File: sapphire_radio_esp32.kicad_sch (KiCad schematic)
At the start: 137 parts, among them IC1 AZ1117CH-3.3TRG1, IC2 AS169-73LF, IC3 CP2102N-A02-GQFN28R, J1 GT-USB-7055E, J2 Screw_Terminal_01x02, J3 FAKRA, J4 Screw_Terminal_01x02, J5 Screw_Terminal_01x02, J6 Conn_01x03, Q1 DMG2305UX-7, Q2 DMP3013SFV-7, Q3 2N7002PS_115, SW1 1825027-8, SW2 1825027-8, SW3 1825027-8, SW4 1825027-8, SW5 1825027-8, SW6 RK09711110EL, U1 ESP32-WROOM-32E-N8R2, U3 NC7WZ14P6X, U4 SI4735, U5 NC7WZ14P6X, U6 TMUX1574PWR, U7 PCM5122PWR, U8 MAX9744ETH_

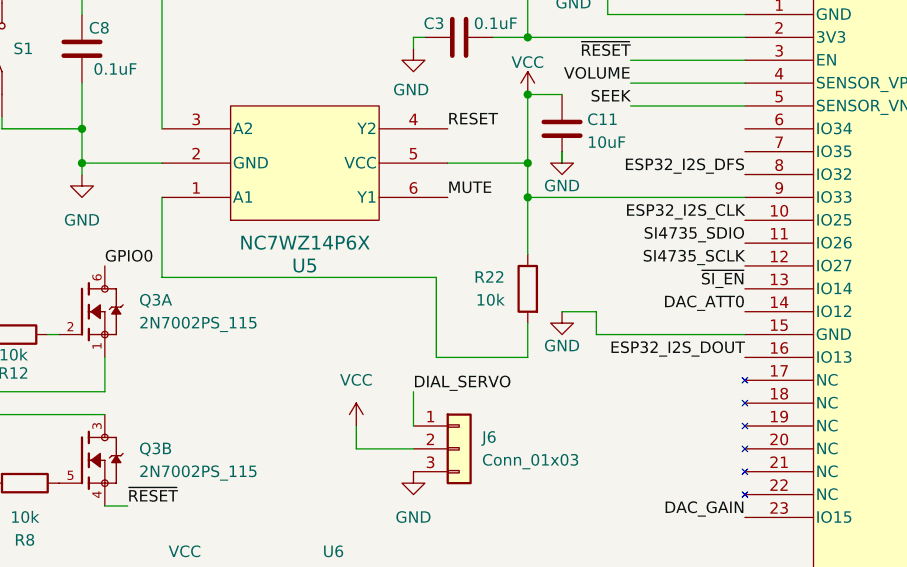
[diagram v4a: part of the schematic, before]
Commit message: Move fakra to board edge; move associated parts; silkscreen
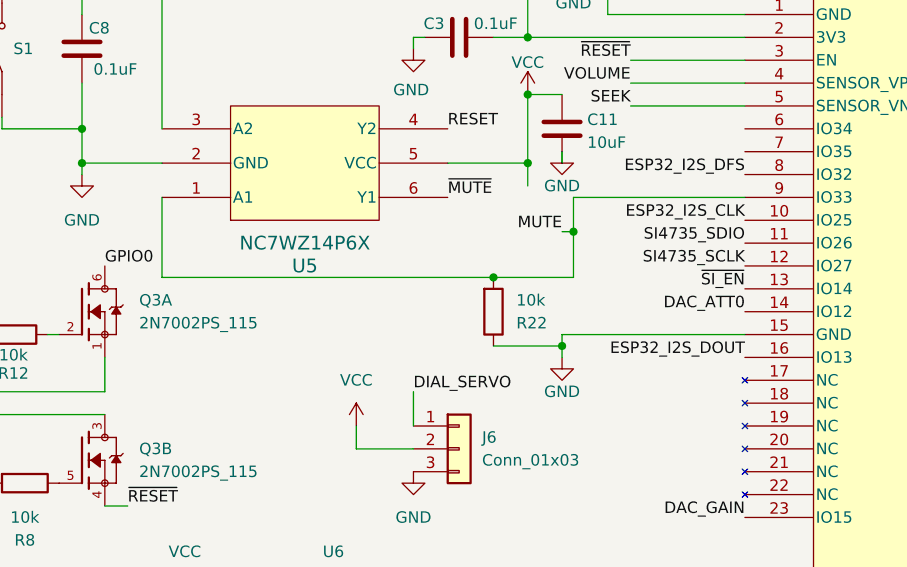
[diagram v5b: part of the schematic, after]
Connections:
- net GND: now also R22.1
- net MUTE: now also R22.2, U1.9 (IO33), U5.1 (A1); no longer U5.6 (Y1)
- net VCC: no longer R22.1, U1.9 (IO33)
- net ~{MUTE}: now also U5.6 (Y1)
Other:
- moved on the sheet: R22
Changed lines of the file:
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@@
 	)
 	(junction
+		(at 76.2 124.46)
+		(diameter 0)
+		(color 0 0 0 0)
+	)
+	(junction
 		(at 80.01 111.76)
 		(diameter 0)
@@
 	)
 	(junction
-		(at 80.01 115.57)
-		(diameter 0)
-		(color 0 0 0 0)
-	)
-	(junction
 		(at 30.48 90.17)
 		(diameter 0)
@@
 	)
 	(junction
+		(at 85.09 119.38)
+		(diameter 0)
+		(color 0 0 0 0)
+	)
+	(junction
 		(at 299.72 17.78)
 		(diameter 0)
@@
 	)
 	(junction
+		(at 83.82 132.08)
+		(diameter 0)
+		(color 0 0 0 0)
+	)
+	(junction
 		(at 167.64 68.58)
 		(diameter 0)
@@
 	(wire
 		(pts
-			(xy 87.63 128.27) (xy 87.63 130.81)
-		)
-		(stroke
-			(width 0)
-			(type default)
-		)
-	)
-	(wire
-		(pts
 			(xy 38.1 43.18) (xy 45.72 43.18)
 		)
@@
 	(wire
 		(pts
+			(xy 83.82 133.35) (xy 83.82 132.08)
+		)
+		(stroke
+			(width 0)
+			(type default)
+		)
+	)
+	(wire
+		(pts
 			(xy 232.41 20.32) (xy 233.68 20.32)
 		)
@@
 	(wire
 		(pts
-			(xy 39.37 124.46) (xy 69.85 124.46)
-		)
-		(stroke
-			(width 0)
-			(type default)
-		)
-	)
-	(wire
-		(pts
-			(xy 69.85 133.35) (xy 80.01 133.35)
+			(xy 203.2 88.9) (xy 213.36 88.9)
 		)
 		(stroke
@@
 	(wire
 		(pts
-			(xy 203.2 88.9) (xy 213.36 88.9)
+			(xy 232.41 33.02) (xy 234.95 33.02)
 		)
 		(stroke
@@
 	(wire
 		(pts
-			(xy 232.41 33.02) (xy 234.95 33.02)
+			(xy 19.05 149.86) (xy 20.32 149.86)
 		)
 		(stroke
@@
 	(wire
 		(pts
-			(xy 19.05 149.86) (xy 20.32 149.86)
+			(xy 270.51 114.3) (xy 265.43 114.3)
 		)
 		(stroke
@@
 	(wire
 		(pts
-			(xy 270.51 114.3) (xy 265.43 114.3)
+			(xy 83.82 130.81) (xy 104.14 130.81)
 		)
 		(stroke
@@
 	(wire
 		(pts
+			(xy 83.82 119.38) (xy 85.09 119.38)
+		)
+		(stroke
+			(width 0)
+			(type default)
+		)
+	)
+	(wire
+		(pts
 			(xy 233.68 179.07) (xy 233.68 177.8)
 		)
@@
 	(wire
 		(pts
-			(xy 80.01 129.54) (xy 80.01 133.35)
-		)
-		(stroke
-			(width 0)
-			(type default)
-		)
-	)
-	(wire
-		(pts
 			(xy 102.87 74.93) (xy 102.87 80.01)
 		)
@@
 	(wire
 		(pts
-			(xy 87.63 130.81) (xy 104.14 130.81)
+			(xy 80.01 104.14) (xy 80.01 111.76)
 		)
 		(stroke
@@
 	(wire
 		(pts
-			(xy 80.01 104.14) (xy 80.01 111.76)
+			(xy 218.44 165.1) (xy 224.79 165.1)
 		)
 		(stroke
@@
 	(wire
 		(pts
-			(xy 218.44 165.1) (xy 224.79 165.1)
+			(xy 220.98 30.48) (xy 224.79 30.48)
 		)
 		(stroke
@@
 	(wire
 		(pts
-			(xy 220.98 30.48) (xy 224.79 30.48)
+			(xy 85.09 119.38) (xy 85.09 124.46)
 		)
 		(stroke
@@
 	(wire
 		(pts
+			(xy 39.37 124.46) (xy 76.2 124.46)
+		)
+		(stroke
+			(width 0)
+			(type default)
+		)
+	)
+	(wire
+		(pts
 			(xy 204.47 86.36) (xy 203.2 86.36)
 		)
@@
 	(wire
 		(pts
-			(xy 69.85 124.46) (xy 69.85 133.35)
-		)
-		(stroke
-			(width 0)
-			(type default)
-		)
-	)
-	(wire
-		(pts
 			(xy 262.89 59.69) (xy 262.89 63.5)
 		)
@@
 	(wire
 		(pts
+			(xy 76.2 124.46) (xy 85.09 124.46)
+		)
+		(stroke
+			(width 0)
+			(type default)
+		)
+	)
+	(wire
+		(pts
 			(xy 314.96 101.6) (xy 321.31 101.6)
 		)
@@
 	(wire
 		(pts
+			(xy 83.82 132.08) (xy 83.82 130.81)
+		)
+		(stroke
+			(width 0)
+			(type default)
+		)
+	)
+	(wire
+		(pts
 			(xy 314.96 93.98) (xy 321.31 93.98)
 		)
@@
 	(wire
 		(pts
-			(xy 80.01 115.57) (xy 104.14 115.57)
-		)
-		(stroke
-			(width 0)
-			(type default)
-		)
-	)
-	(wire
-		(pts
 			(xy 213.36 80.01) (xy 213.36 86.36)
 		)
@@
 	(wire
 		(pts
-			(xy 83.82 128.27) (xy 87.63 128.27)
-		)
-		(stroke
-			(width 0)
-			(type default)
-		)
-	)
-	(wire
-		(pts
 			(xy 233.68 40.64) (xy 233.68 38.1)
 		)
@@
 	(wire
 		(pts
-			(xy 80.01 111.76) (xy 80.01 115.57)
-		)
-		(stroke
-			(width 0)
-			(type default)
-		)
-	)
-	(wire
-		(pts
 			(xy 180.34 190.5) (xy 180.34 200.66)
 		)
@@
 	(wire
 		(pts
+			(xy 76.2 132.08) (xy 83.82 132.08)
+		)
+		(stroke
+			(width 0)
+			(type default)
+		)
+	)
+	(wire
+		(pts
 			(xy 76.2 97.79) (xy 80.01 97.79)
 		)
@@
 	(wire
 		(pts
-			(xy 80.01 115.57) (xy 80.01 121.92)
+			(xy 104.14 115.57) (xy 85.09 115.57)
+		)
+		(stroke
+			(width 0)
+			(type default)
+		)
+	)
+	(wire
+		(pts
+			(xy 80.01 111.76) (xy 80.01 114.3)
 		)
 		(stroke
@@
 	(wire
 		(pts
+			(xy 85.09 115.57) (xy 85.09 119.38)
+		)
+		(stroke
+			(width 0)
+			(type default)
+		)
+	)
+	(wire
+		(pts
 			(xy 128.27 185.42) (xy 138.43 185.42)
 		)
@@
 	)
 	(label "MUTE"
-		(at 71.12 115.57 0)
+		(at 83.82 119.38 180)
 		(effects
 			(font
 				(size 1.27 1.27)
 			)
-			(justify left bottom)
+			(justify right bottom)
 		)
 	)
@@
 		)
 	)
+	(label "~{MUTE}"
+		(at 71.12 115.57 0)
+		(effects
+			(font
+				(size 1.27 1.27)
+			)
+			(justify left bottom)
+		)
+	)
 	(label "B3"
 		(at 321.31 27.94 180)
@@
 	(symbol
 		(lib_id "power:GND")
-		(at 83.82 128.27 0)
+		(at 83.82 133.35 0)
 		(unit 1)
 		(exclude_from_sim no)
@@
 		(dnp no)
 		(property "Reference" "#PWR091"
-			(at 83.82 134.62 0)
+			(at 83.82 139.7 0)
 			(effects
 				(font
@@
 		)
 		(property "Value" "GND"
-			(at 83.82 132.08 0)
+			(at 83.82 137.16 0)
 			(effects
 				(font
@@
 		)
 		(property "Footprint" ""
-			(at 83.82 128.27 0)
+			(at 83.82 133.35 0)
 			(effects
 				(font
@@
 		)
 		(property "Datasheet" ""
-			(at 83.82 128.27 0)
+			(at 83.82 133.35 0)
 			(effects
 				(font
@@
 		)
 		(property "Description" "Power symbol creates a global label with name \"GND\" , ground"
-			(at 83.82 128.27 0)
+			(at 83.82 133.35 0)
 			(effects
 				(font
@@
 	(symbol
 		(lib_id "Device:R")
-		(at 80.01 125.73 0)
-		(mirror y)
+		(at 76.2 128.27 0)
+		(mirror x)
 		(unit 1)
 		(exclude_from_sim no)
@@
 		(dnp no)
 		(property "Reference" "R22"
-			(at 77.47 124.4599 0)
+			(at 78.74 129.5401 0)
 			(effects
 				(font
@@
 		)
 		(property "Value" "10k"
-			(at 77.47 126.9999 0)
+			(at 78.74 127.0001 0)
 			(effects
 				(font
@@
 		)
 		(property "Footprint" "Resistor_SMD:R_0603_1608Metric"
-			(at 81.788 125.73 90)
+			(at 74.422 128.27 90)
 			(effects
 				(font
@@
 		)
 		(property "Datasheet" "~"
-			(at 80.01 125.73 0)
+			(at 76.2 128.27 0)
 			(effects
 				(font
@@
 		)
 		(property "Description" "Resistor"
-			(at 80.01 125.73 0)
+			(at 76.2 128.27 0)
 			(effects
 				(font
